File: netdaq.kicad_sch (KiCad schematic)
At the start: 4 parts

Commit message: fixed couple of things
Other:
- sheet ADC1 ports: added ADCIN[0..7]; removed GPIO[0..7]
- sheet ADC2 ports: added ADCIN[0..7]; removed GPIO[0..7]
- sheet ADC3 ports: added ADCIN[0..7]; removed GPIO[0..7]
- sheet ADC4 ports: added ADCIN[0..7]; removed GPIO[0..7]
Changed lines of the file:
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@@
+	(bus
+		(pts
+			(xy 254 217.17) (xy 254 236.22)
+		)
+		(stroke
+			(width 0)
+			(type default)
+		)
+	)
 	(bus
 		(pts
@@
 	(bus
 		(pts
-			(xy 198.12 215.9) (xy 198.12 233.68)
-		)
-		(stroke
-			(width 0)
-			(type default)
-		)
-	)
-	(bus
-		(pts
 			(xy 232.41 118.11) (xy 303.53 118.11)
 		)
@@
 	(bus
 		(pts
+			(xy 170.18 217.17) (xy 170.18 236.22)
+		)
+		(stroke
+			(width 0)
+			(type default)
+		)
+	)
+	(bus
+		(pts
 			(xy 121.92 45.72) (xy 121.92 113.03)
 		)
@@
 	(bus
 		(pts
-			(xy 254 215.9) (xy 254 236.22)
-		)
-		(stroke
-			(width 0)
-			(type default)
-		)
-	)
-	(bus
-		(pts
 			(xy 204.47 242.57) (xy 204.47 236.22)
 		)
@@
 	(bus
 		(pts
+			(xy 226.06 217.17) (xy 226.06 233.68)
+		)
+		(stroke
+			(width 0)
+			(type default)
+		)
+	)
+	(bus
+		(pts
 			(xy 232.41 115.57) (xy 303.53 115.57)
 		)
@@
 	(bus
 		(pts
+			(xy 198.12 217.17) (xy 198.12 233.68)
+		)
+		(stroke
+			(width 0)
+			(type default)
+		)
+	)
+	(bus
+		(pts
 			(xy 232.41 102.87) (xy 269.24 102.87)
 		)
@@
 		)
 	)
-	(bus
-		(pts
-			(xy 170.18 215.9) (xy 170.18 236.22)
-		)
-		(stroke
-			(width 0)
-			(type default)
-		)
-	)
 	(wire
 		(pts
@@
 	(bus
 		(pts
-			(xy 226.06 215.9) (xy 226.06 233.68)
-		)
-		(stroke
-			(width 0)
-			(type default)
-		)
-	)
-	(bus
-		(pts
 			(xy 215.9 242.57) (xy 215.9 236.22)
 		)
@@
 		)
 	)
-	(label "GPIO[25..32]"
-		(at 254 228.6 90)
+	(label "ADCIN[25..32]"
+		(at 254 232.41 90)
 		(effects
 			(font
@@
 		)
 	)
-	(label "GPIO[17..24]"
-		(at 226.06 228.6 90)
+	(label "ADCIN[17..24]"
+		(at 226.06 232.41 90)
 		(effects
 			(font
@@
 		)
 	)
-	(label "GPIO[9..16]"
-		(at 198.12 228.6 90)
+	(label "ADCIN[9..16]"
+		(at 198.12 232.41 90)
 		(effects
 			(font
@@
 		)
 	)
-	(label "GPIO[1..8]"
-		(at 170.18 228.6 90)
+	(label "ADCIN[1..8]"
+		(at 170.18 232.41 90)
 		(effects
 			(font
@@
 	(sheet
 		(at 190.5 194.31)
-		(size 15.24 21.59)
+		(size 15.24 22.86)
 		(exclude_from_sim no)
 		(in_bom yes)
@@
 			)
 		)
-		(pin "GPIO[0..7]" bidirectional
-			(at 198.12 215.9 270)
-			(effects
-				(font
-					(size 1.27 1.27)
-				)
-				(justify left)
-			)
-		)
 		(pin "SPI{SPI}" bidirectional
 			(at 198.12 194.31 90)
@@
 				)
 				(justify right)
+			)
+		)
+		(pin "ADCIN[0..7]" bidirectional
+			(at 198.12 217.17 270)
+			(effects
+				(font
+					(size 1.27 1.27)
+				)
+				(justify left)
 			)
 		)
@@
 	(sheet
 		(at 218.44 194.31)
-		(size 15.24 21.59)
+		(size 15.24 22.86)
 		(exclude_from_sim no)
 		(in_bom yes)
@@
 			)
 		)
-		(pin "GPIO[0..7]" bidirectional
-			(at 226.06 215.9 270)
-			(effects
-				(font
-					(size 1.27 1.27)
-				)
-				(justify left)
-			)
-		)
 		(pin "SPI{SPI}" bidirectional
 			(at 226.06 194.31 90)
@@
 				)
 				(justify right)
+			)
+		)
+		(pin "ADCIN[0..7]" bidirectional
+			(at 226.06 217.17 270)
+			(effects
+				(font
+					(size 1.27 1.27)
+				)
+				(justify left)
 			)
 		)
@@
 	(sheet
 		(at 162.56 194.31)
-		(size 15.24 21.59)
+		(size 15.24 22.86)
 		(exclude_from_sim no)
 		(in_bom yes)
@@
 			)
 		)
-		(pin "GPIO[0..7]" bidirectional
-			(at 170.18 215.9 270)
-			(effects
-				(font
-					(size 1.27 1.27)
-				)
-				(justify left)
-			)
-		)
 		(pin "SPI{SPI}" bidirectional
 			(at 170.18 194.31 90)
@@
 				)
 				(justify right)
+			)
+		)
+		(pin "ADCIN[0..7]" bidirectional
+			(at 170.18 217.17 270)
+			(effects
+				(font
+					(size 1.27 1.27)
+				)
+				(justify left)
 			)
 		)
@@
 	(sheet
 		(at 246.38 194.31)
-		(size 15.24 21.59)
+		(size 15.24 22.86)
 		(exclude_from_sim no)
 		(in_bom yes)
@@
 			)
 		)
-		(pin "GPIO[0..7]" bidirectional
-			(at 254 215.9 270)
-			(effects
-				(font
-					(size 1.27 1.27)
-				)
-				(justify left)
-			)
-		)
 		(pin "SPI{SPI}" bidirectional
 			(at 254 194.31 90)
@@
 			)
 		)
+		(pin "ADCIN[0..7]" bidirectional
+			(at 254 217.17 270)
+			(effects
+				(font
+					(size 1.27 1.27)
+				)
+				(justify left)
+			)
+		)

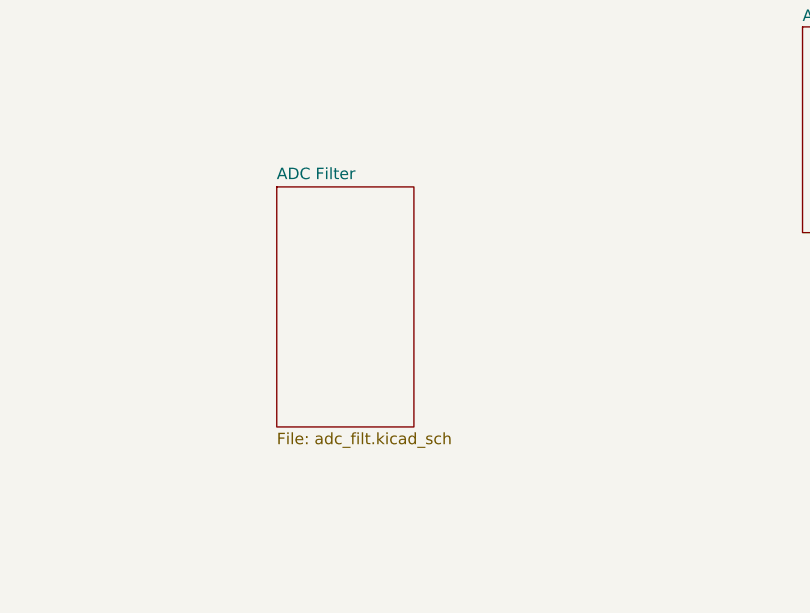
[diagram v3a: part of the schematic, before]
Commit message: fixed some issues, preliminary layout on adc input filter/scaling
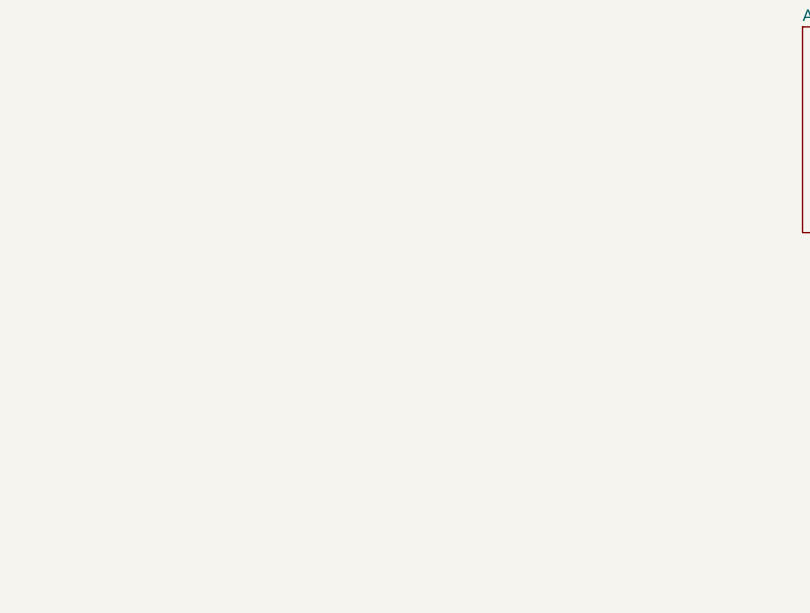
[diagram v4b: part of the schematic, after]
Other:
- removed sheet ADC Filter
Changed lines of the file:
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@@
-	)
-	(sheet
-		(at 104.14 212.09)
-		(size 15.24 26.67)
-		(exclude_from_sim no)
-		(in_bom yes)
-		(on_board yes)
-		(dnp no)
-		(fields_autoplaced yes)
-		(stroke
-			(width 0.1524)
-			(type solid)
-		)
-		(fill
-			(color 0 0 0 0)
-		)
-		(property "Sheetname" "ADC Filter"
-			(at 104.14 211.3784 0)
-			(show_name no)
-			(do_not_autoplace no)
-			(effects
-				(font
-					(size 1.27 1.27)
-				)
-				(justify left bottom)
-			)
-		)
-		(property "Sheetfile" "adc_filt.kicad_sch"
-			(at 104.14 239.3446 0)
-			(show_name no)
-			(do_not_autoplace no)
-			(effects
-				(font
-					(size 1.27 1.27)
-				)
-				(justify left top)
-			)
-		)
-		(instances
-			(project "netdaq"
-				(path "/2970f661-65ab-4e2b-aeda-d76d1044f2b8"
-					(page "16")
-				)
-			)
-		)
 	)
 	(sheet

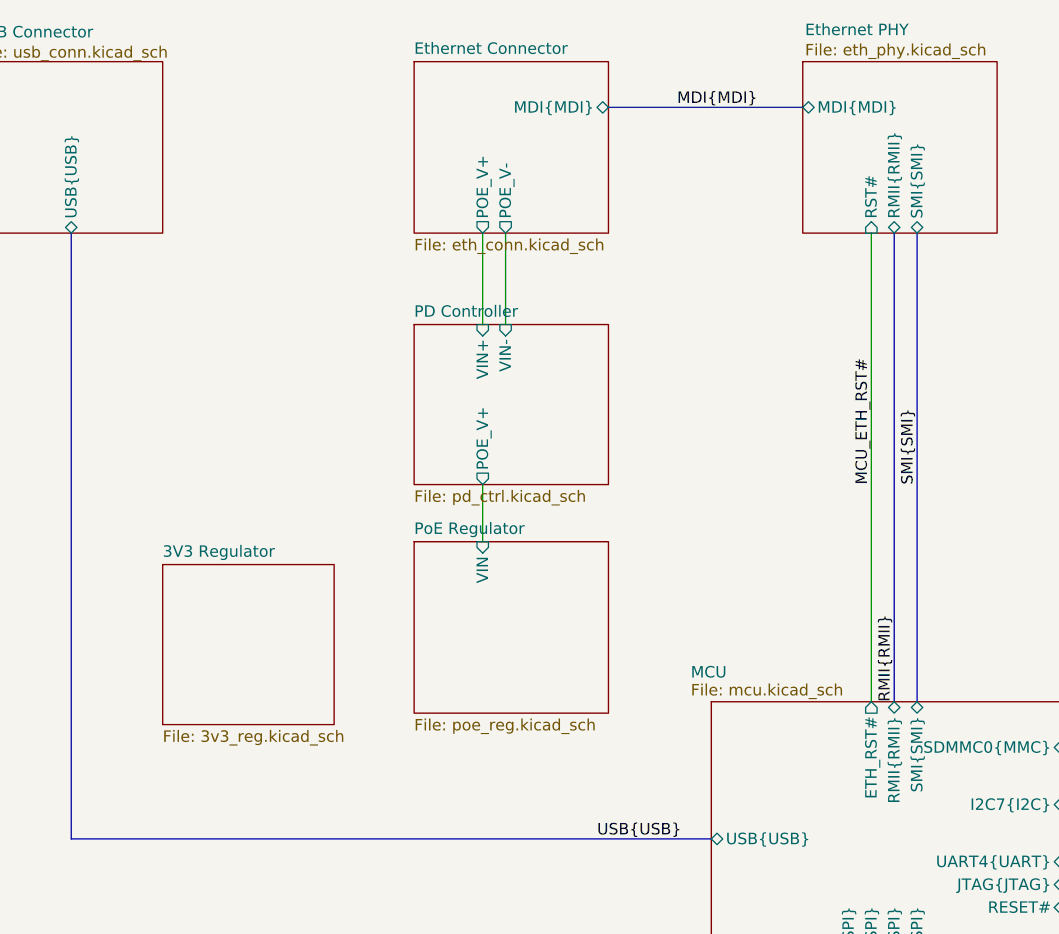
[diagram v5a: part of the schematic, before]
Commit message: fixed some more schematic review
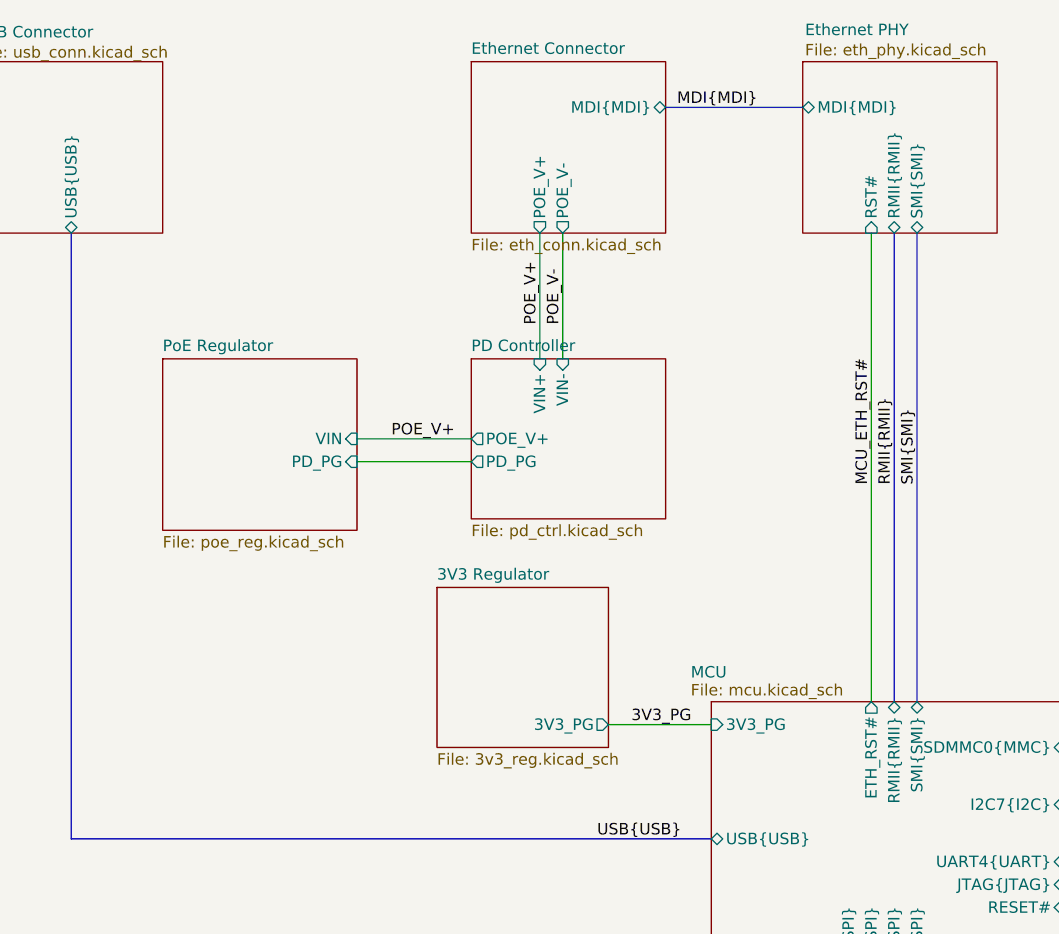
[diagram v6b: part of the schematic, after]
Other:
- sheet 3V3 Regulator ports: added 3V3_PG; removed none
- sheet MCU ports: added 3V3_PG; removed none
- sheet PD Controller ports: added PD_PG; removed none
- sheet PoE Regulator ports: added PD_PG; removed none

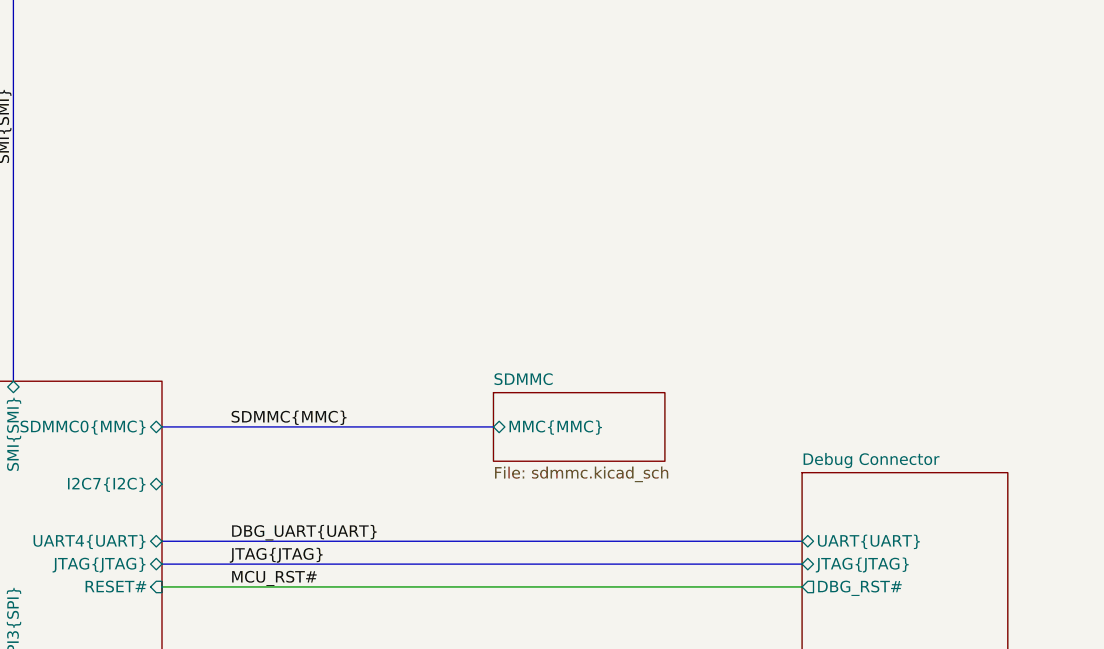
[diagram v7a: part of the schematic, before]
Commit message: added eeprom
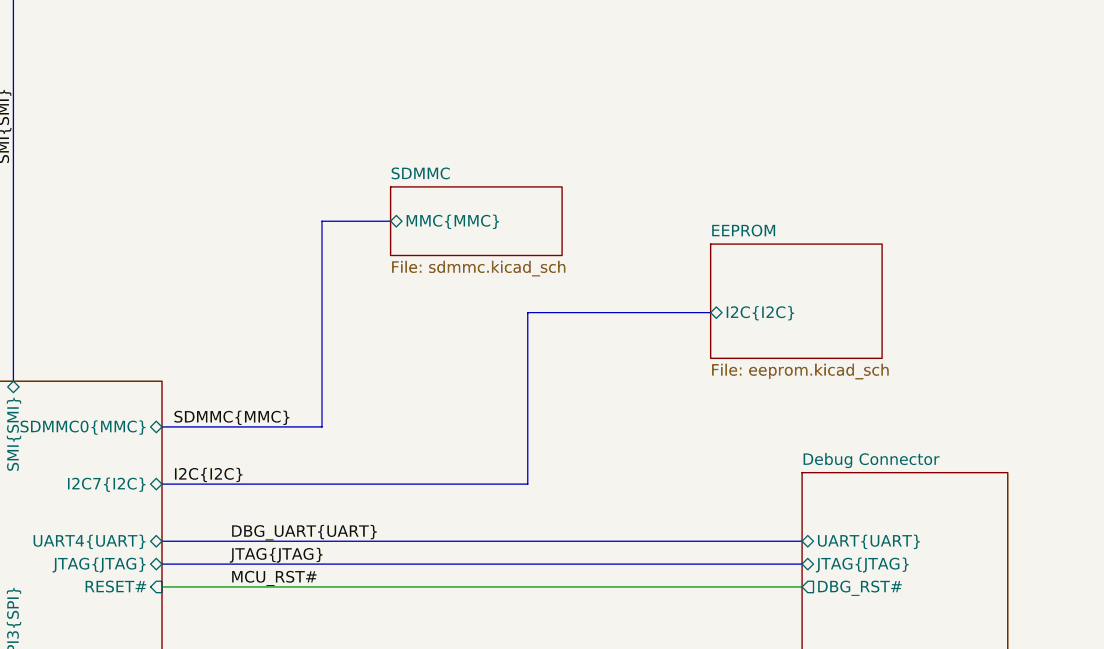
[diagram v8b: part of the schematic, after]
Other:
- added sheet EEPROM (eeprom.kicad_sch)
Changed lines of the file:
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@@
+	(bus
+		(pts
+			(xy 250.19 80.01) (xy 250.19 102.87)
+		)
+		(stroke
+			(width 0)
+			(type default)
+		)
+	)
 	(bus
 		(pts
@@
 	(bus
 		(pts
+			(xy 273.05 109.22) (xy 273.05 90.17)
+		)
+		(stroke
+			(width 0)
+			(type default)
+		)
+	)
+	(bus
+		(pts
 			(xy 208.28 242.57) (xy 208.28 233.68)
 		)
@@
 	(bus
 		(pts
+			(xy 232.41 109.22) (xy 273.05 109.22)
+		)
+		(stroke
+			(width 0)
+			(type default)
+		)
+	)
+	(bus
+		(pts
 			(xy 226.06 217.17) (xy 226.06 233.68)
 		)
@@
 	(bus
 		(pts
-			(xy 232.41 102.87) (xy 269.24 102.87)
+			(xy 250.19 80.01) (xy 257.81 80.01)
 		)
 		(stroke
@@
 	(bus
 		(pts
+			(xy 250.19 102.87) (xy 232.41 102.87)
+		)
+		(stroke
+			(width 0)
+			(type default)
+		)
+	)
+	(bus
+		(pts
 			(xy 121.92 113.03) (xy 193.04 113.03)
 		)
@@
 	(bus
 		(pts
+			(xy 273.05 90.17) (xy 293.37 90.17)
+		)
+		(stroke
+			(width 0)
+			(type default)
+		)
+	)
+	(bus
+		(pts
 			(xy 215.9 45.72) (xy 215.9 97.79)
 		)
@@
 			(width 0)
 			(type default)
+		)
+	)
+	(label "I2C{I2C}"
+		(at 233.68 109.22 0)
+		(effects
+			(font
+				(size 1.27 1.27)
+			)
+			(justify left bottom)
 		)
 	)
@@
 	)
 	(label "SDMMC{MMC}"
-		(at 240.03 102.87 0)
+		(at 233.68 102.87 0)
 		(effects
 			(font
@@
 	)
 	(sheet
-		(at 269.24 99.06)
+		(at 257.81 76.2)
 		(size 19.05 7.62)
 		(exclude_from_sim no)
@@
 		)
 		(property "Sheetname" "SDMMC"
-			(at 269.24 98.3484 0)
+			(at 257.81 75.4884 0)
 			(show_name no)
 			(do_not_autoplace no)
@@
 		)
 		(property "Sheetfile" "sdmmc.kicad_sch"
-			(at 269.24 107.2646 0)
+			(at 257.81 84.4046 0)
 			(show_name no)
 			(do_not_autoplace no)
@@
 		)
 		(property "Field2" ""
-			(at 269.24 99.06 0)
+			(at 257.81 76.2 0)
 			(show_name no)
 			(do_not_autoplace no)
@@
 		)
 		(pin "MMC{MMC}" bidirectional
-			(at 269.24 102.87 180)
+			(at 257.81 80.01 180)
 			(effects
 				(font
@@
 				)
 			)
+		)
+	)
+	(sheet
+		(at 293.37 82.55)
+		(size 19.05 12.7)
+		(exclude_from_sim no)
+		(in_bom yes)
+		(on_board yes)
+		(dnp no)
+		(fields_autoplaced yes)
+		(stroke
+			(width 0.1524)
+			(type solid)
+		)
+		(fill
+			(color 0 0 0 0)
+		)
+		(property "Sheetname" "EEPROM"
+			(at 293.37 81.8384 0)
+			(show_name no)
+			(do_not_autoplace no)
+			(effects
+				(font
+					(size 1.27 1.27)
+				)
+				(justify left bottom)
+			)
+		)
+		(property "Sheetfile" "eeprom.kicad_sch"
+			(at 293.37 95.8346 0)
+			(show_name no)
+			(do_not_autoplace no)
+			(effects
+				(font
+					(size 1.27 1.27)
+				)
+				(justify left top)
+			)
+		)
+		(pin "I2C{I2C}" bidirectional
+			(at 293.37 90.17 180)
+			(effects
+				(font
+					(size 1.27 1.27)
+				)
+				(justify left)
+			)
+		)
+		(instances
+			(project "netdaq"
+				(path "/2970f661-65ab-4e2b-aeda-d76d1044f2b8"
+					(page "16")
+				)
+			)
